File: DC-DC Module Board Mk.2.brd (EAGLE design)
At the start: 177.9 x 101.7 mm, 151 parts, among them T1 FDN340P, T2 AP1117_LIN_REG, U3 LM1085IS-5.0

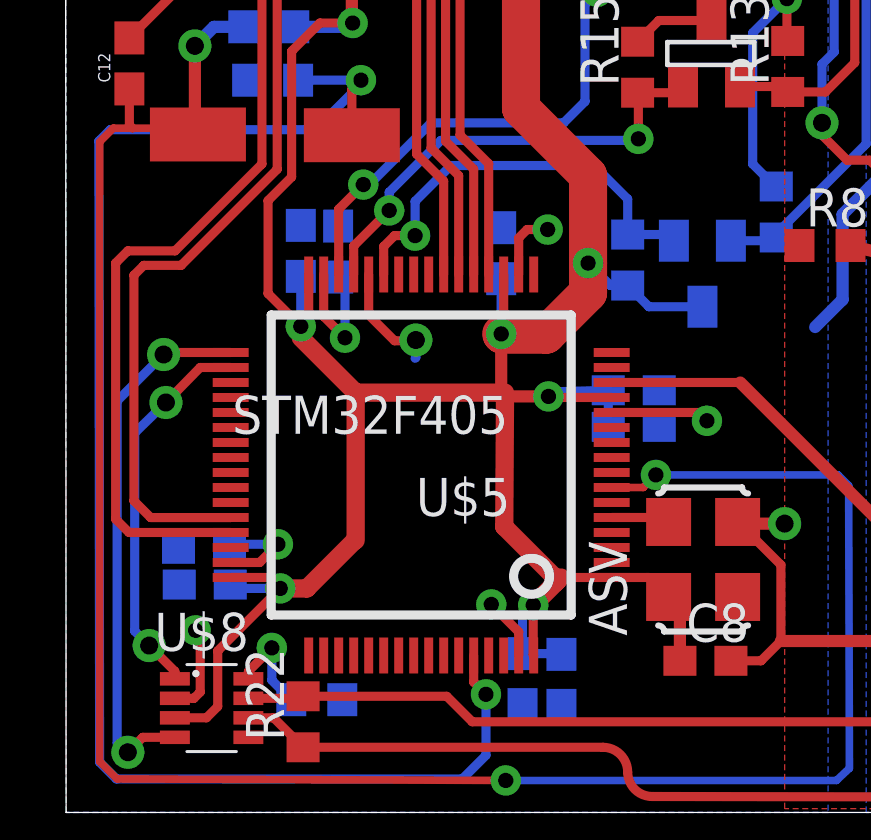
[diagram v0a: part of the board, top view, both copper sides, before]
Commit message: Changed pins for i2c
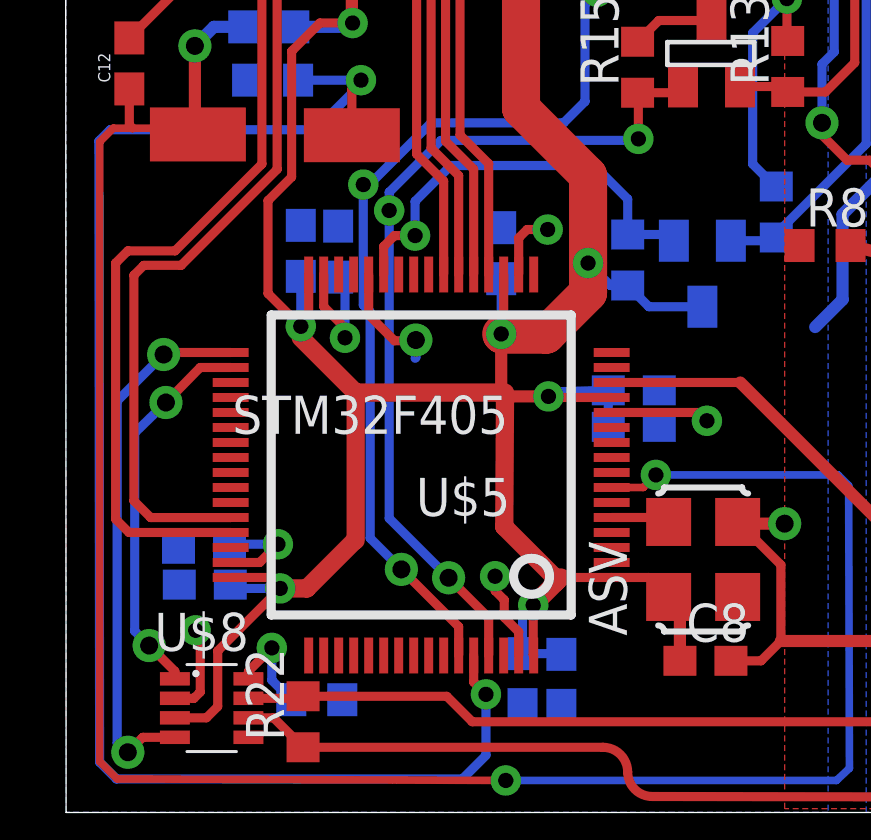
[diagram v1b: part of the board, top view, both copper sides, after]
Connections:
- removed net PB7: U$5.59
- removed net PIN61: U$5.61
- new net PB10: U$5.29
- new net PB11: U$5.30
- net SCL1: now also U$5.61; no longer U$5.29
- net SDA1: now also U$5.59; no longer U$5.30
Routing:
- net SCL1: track 15.6 -> 29.2 mm, vias 2 -> 3
- net SDA1: track 19.5 -> 33.0 mm, vias 2 -> 3
- net DGND: track 462.5 -> 463.4 mm
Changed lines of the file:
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@@
 <?xml version="1.0" encoding="utf-8"?>
 <!DOCTYPE eagle SYSTEM "eagle.dtd">
-<eagle version="7.4.0">
+<eagle version="7.5.0">
 <drawing>
 <settings>
@@
 <wire x1="4.15" y1="31.72" x2="4.15" y2="30.52" width="0.4064" layer="1"/>
 <wire x1="1.45" y1="32.02" x2="1.45" y2="34.02" width="0.4064" layer="1"/>
-<via x="14.1732" y="5.6642" extent="1-16" drill="0.508"/>
+<via x="14.3002" y="6.604" extent="1-16" drill="0.508"/>
 <wire x1="15.0864" y1="3.9624" x2="15.0864" y2="4.751" width="0.3048" layer="1"/>
-<wire x1="15.0864" y1="4.751" x2="14.1732" y2="5.6642" width="0.3048" layer="1"/>
 <wire x1="1.79" y1="39.2938" x2="1.79" y2="41.0718" width="0.3048" layer="1"/>
 <wire x1="1.79" y1="41.0718" x2="1.79" y2="42.8498" width="0.3048" layer="1"/>
@@
 <wire x1="109.9566" y1="6.1722" x2="109.982" y2="6.1976" width="0.4064" layer="1"/>
 <wire x1="109.982" y1="6.1976" x2="114.9096" y2="6.1976" width="0.4064" layer="1"/>
+<wire x1="15.0864" y1="4.751" x2="14.605" y2="5.2324" width="0.3048" layer="1"/>
+<wire x1="14.605" y1="5.2324" x2="14.605" y2="5.8166" width="0.3048" layer="1"/>
+<wire x1="14.605" y1="5.8166" x2="14.3002" y2="6.1214" width="0.3048" layer="1"/>
+<wire x1="14.3002" y1="6.1214" x2="14.3002" y2="6.604" width="0.3048" layer="1"/>
 </signal>
 <signal name="VCAP_1">
@@
 <wire x1="9.2964" y1="16.3458" x2="9.2964" y2="14.5542" width="0.3048" layer="16"/>
 <via x="9.2964" y="14.5542" extent="1-16" drill="0.508"/>
-<wire x1="9.2964" y1="14.5542" x2="8.5864" y2="15.2642" width="0.3048" layer="1"/>
-<wire x1="8.5864" y1="15.2642" x2="8.5864" y2="16.6624" width="0.3048" layer="1"/>
+<wire x1="8.5864" y1="16.6624" x2="8.5864" y2="15.5944" width="0.3048" layer="1"/>
+<wire x1="8.5864" y1="15.5944" x2="9.2964" y2="14.8844" width="0.3048" layer="1"/>
+<wire x1="9.2964" y1="14.8844" x2="9.2964" y2="14.5542" width="0.3048" layer="1"/>
 </signal>
 <signal name="VCAP_2">
@@
 <contactref element="U$5" pad="57"/>
 </signal>
-<signal name="PIN61">
-<contactref element="U$5" pad="61"/>
-</signal>
 <signal name="PIN62">
 <contactref element="U$5" pad="62"/>
@@
 <contactref element="U$9" pad="3"/>
 <contactref element="R16" pad="1"/>
-<contactref element="U$5" pad="30"/>
-<wire x1="9.0864" y1="16.6624" x2="9.0864" y2="18.84" width="0.3048" layer="1"/>
-<wire x1="9.0864" y1="18.84" x2="9.906" y2="19.6596" width="0.3048" layer="1"/>
 <via x="9.906" y="19.6596" extent="1-16" drill="0.508"/>
 <wire x1="19.2532" y1="27.5472" x2="20.636" y2="27.5472" width="0.3048" layer="1"/>
@@
 <wire x1="17.7038" y1="26.0858" x2="17.7918" y2="26.0858" width="0.3048" layer="1"/>
 <wire x1="17.7918" y1="26.0858" x2="19.2532" y2="27.5472" width="0.3048" layer="1"/>
-<wire x1="9.906" y1="19.6596" x2="10.1092" y2="19.6596" width="0.3048" layer="16"/>
 <wire x1="10.1092" y1="19.6596" x2="12.1666" y2="21.717" width="0.3048" layer="16"/>
 <wire x1="12.1666" y1="21.717" x2="16.5862" y2="21.717" width="0.3048" layer="16"/>
 <wire x1="16.5862" y1="21.717" x2="17.2974" y2="22.4282" width="0.3048" layer="16"/>
+<contactref element="U$5" pad="59"/>
+<wire x1="13.0864" y1="3.9624" x2="13.0864" y2="4.9222" width="0.3048" layer="1"/>
+<wire x1="13.0864" y1="4.9222" x2="11.176" y2="6.8326" width="0.3048" layer="1"/>
+<via x="11.176" y="6.8326" extent="1-16" drill="0.6"/>
+<wire x1="11.176" y1="6.8326" x2="10.1346" y2="7.874" width="0.3048" layer="16"/>
+<wire x1="10.1346" y1="7.874" x2="10.1346" y2="15.4178" width="0.3048" layer="16"/>
+<wire x1="10.1346" y1="15.4178" x2="9.906" y2="15.6464" width="0.3048" layer="16"/>
+<wire x1="9.906" y1="15.6464" x2="9.906" y2="19.6596" width="0.3048" layer="16"/>
+<wire x1="9.906" y1="19.6596" x2="10.1092" y2="19.6596" width="0" layer="19" extent="16-16"/>
 </signal>
 <signal name="SCL1">
 <contactref element="BSS138" pad="3"/>
 <contactref element="R15" pad="1"/>
-<contactref element="U$5" pad="29"/>
-<wire x1="9.5864" y1="16.6624" x2="9.5864" y2="17.6128" width="0.3048" layer="1"/>
-<wire x1="9.5864" y1="17.6128" x2="10.7696" y2="18.796" width="0.3048" layer="1"/>
 <via x="10.7696" y="18.796" extent="1-16" drill="0.508"/>
 <wire x1="19.05" y1="22.7212" x2="19.1906" y2="22.7212" width="0.3048" layer="1"/>
@@
 <wire x1="12.4968" y1="21.1328" x2="19.0246" y2="21.1328" width="0.3048" layer="16"/>
 <wire x1="19.0246" y1="21.1328" x2="19.0754" y2="21.1836" width="0.3048" layer="16"/>
+<contactref element="U$5" pad="61"/>
+<wire x1="14.0864" y1="3.9624" x2="14.0864" y2="5.2176" width="0.3048" layer="1"/>
+<wire x1="14.0864" y1="5.2176" x2="12.7508" y2="6.5532" width="0.3048" layer="1"/>
+<via x="12.7508" y="6.5532" extent="1-16" drill="0.6"/>
+<wire x1="12.7508" y1="6.5532" x2="10.7696" y2="8.5344" width="0.3048" layer="16"/>
+<wire x1="10.7696" y1="8.5344" x2="10.7696" y2="18.796" width="0.3048" layer="16"/>
 </signal>
 <signal name="N$63">
@@
 <contactref element="U$5" pad="58"/>
 </signal>
-<signal name="PB7">
-<contactref element="U$5" pad="59"/>
+<signal name="PB10">
+<contactref element="U$5" pad="29"/>
+</signal>
+<signal name="PB11">
+<contactref element="U$5" pad="30"/>
 </signal>
 </signals>

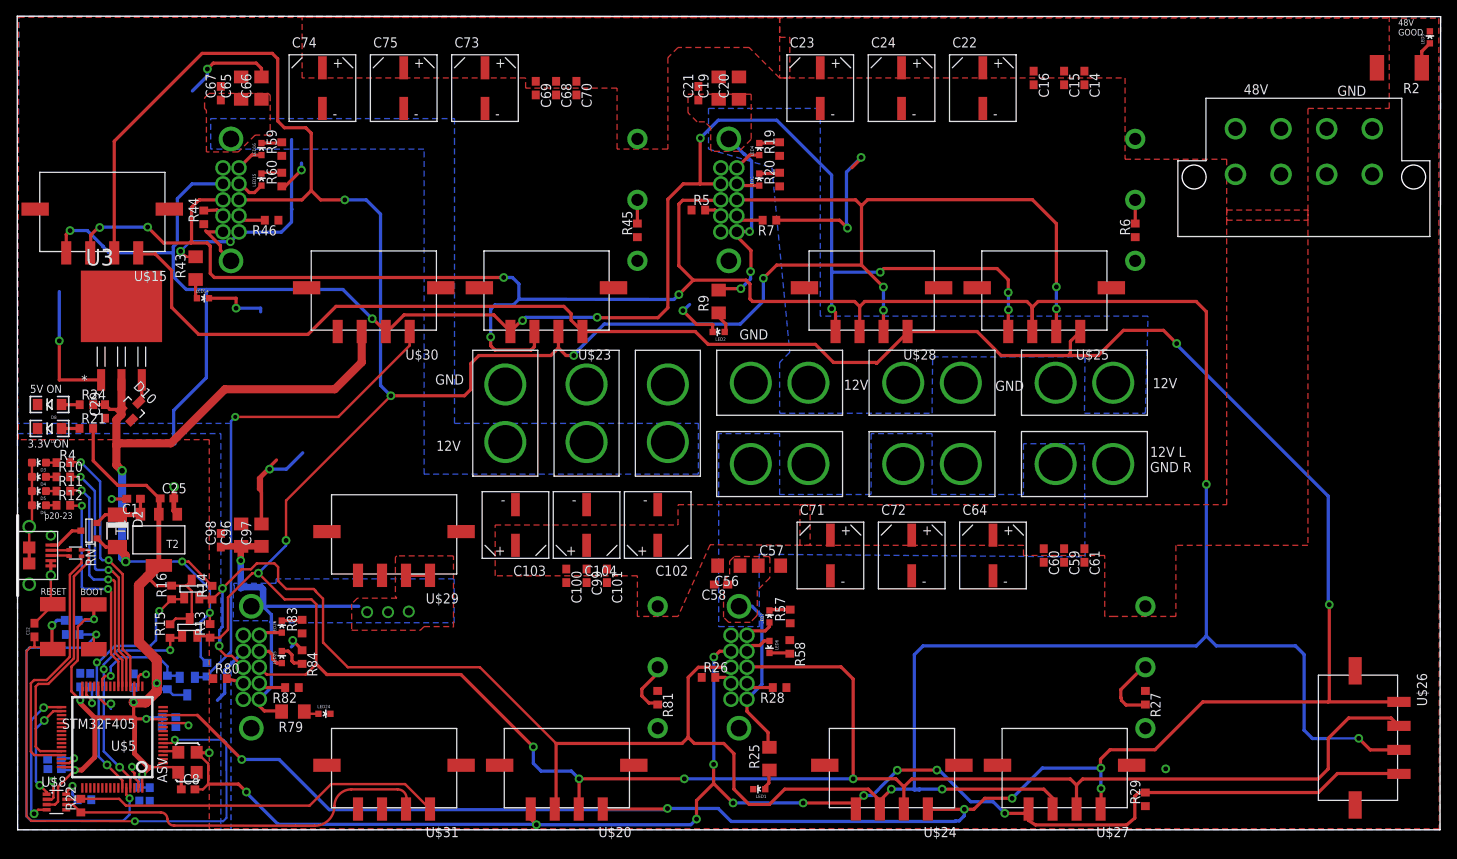
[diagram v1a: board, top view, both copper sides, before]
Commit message: Added GND vias around the board
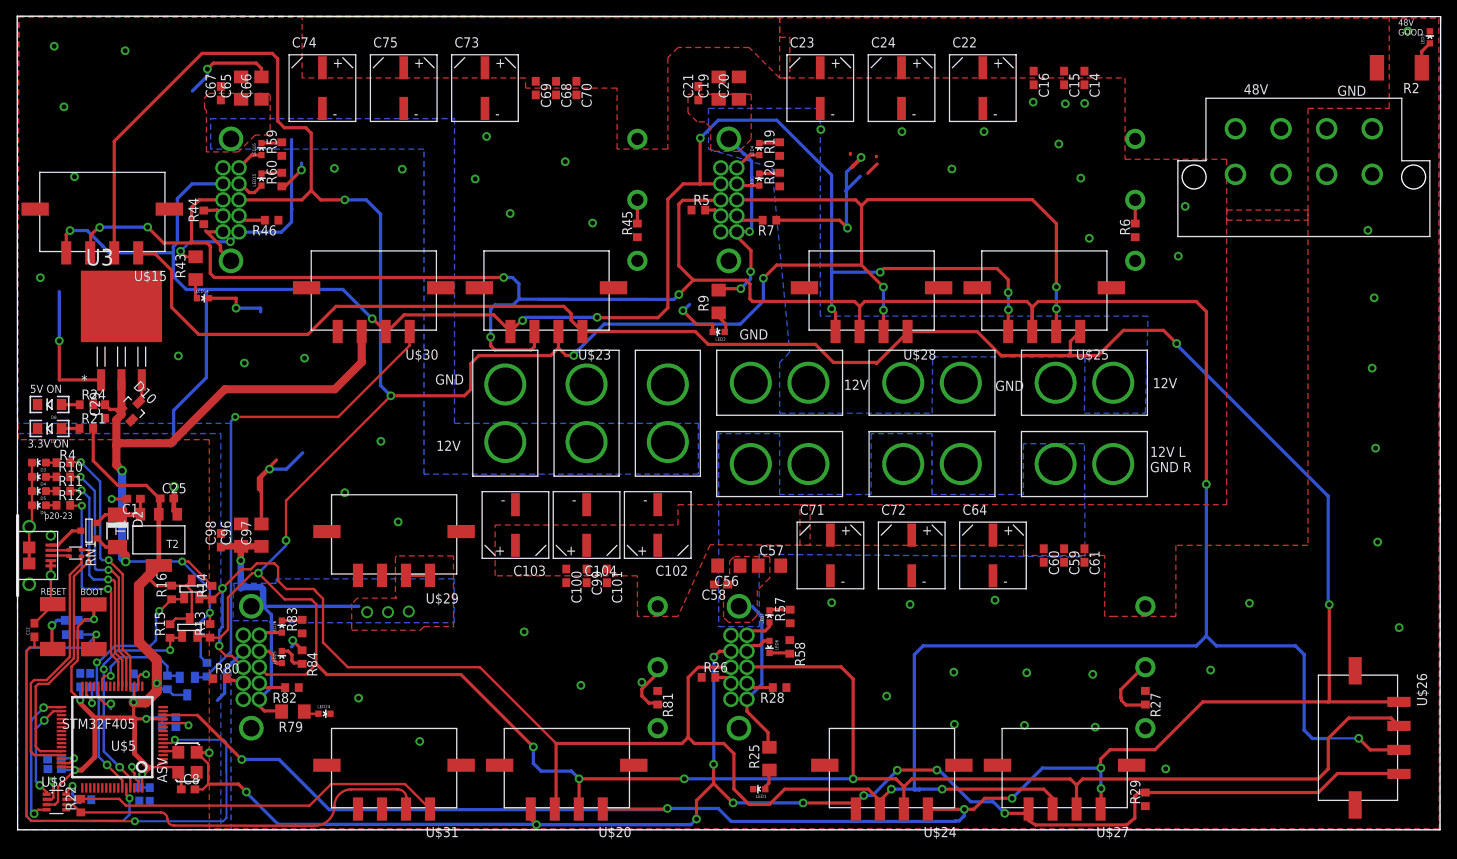
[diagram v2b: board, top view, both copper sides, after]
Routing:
- net GND: track 98.9 -> 105.1 mm, vias 9 -> 62
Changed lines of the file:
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@@
 <wire x1="103.6066" y1="80.9498" x2="105.4354" y2="82.7786" width="0.4064" layer="16"/>
 <via x="105.4354" y="82.7786" extent="1-16" drill="0.6"/>
-<wire x1="105.4354" y1="82.7786" x2="105.4354" y2="82.6516" width="0.4064" layer="1"/>
+<wire x1="105.4354" y1="82.7786" x2="105.4354" y2="82.7024" width="0.4064" layer="1"/>
+<wire x1="105.4354" y1="82.7024" x2="105.4354" y2="82.6516" width="0.4064" layer="1"/>
 <wire x1="105.4354" y1="82.6516" x2="104.267" y2="81.4832" width="0.4064" layer="1"/>
+<via x="45.4152" y="47.2948" extent="1-16" drill="0.6"/>
+<via x="40.894" y="40.8686" extent="1-16" drill="0.6"/>
+<via x="47.5742" y="37.211" extent="1-16" drill="0.6"/>
+<via x="63.3222" y="23.4696" extent="1-16" drill="0.6"/>
+<via x="70.4088" y="16.7894" extent="1-16" drill="0.6"/>
+<via x="42.6212" y="15.1892" extent="1-16" drill="0.6"/>
+<via x="50.2666" y="9.779" extent="1-16" drill="0.6"/>
+<via x="101.7524" y="27.1272" extent="1-16" drill="0.6"/>
+<via x="111.5568" y="26.8986" extent="1-16" drill="0.6"/>
+<via x="122.174" y="27.432" extent="1-16" drill="0.6"/>
+<via x="108.6358" y="15.4432" extent="1-16" drill="0.6"/>
+<via x="117.0178" y="18.4404" extent="1-16" drill="0.6"/>
+<via x="126.1364" y="18.3642" extent="1-16" drill="0.6"/>
+<via x="134.3914" y="18.161" extent="1-16" drill="0.6"/>
+<via x="117.094" y="11.9126" extent="1-16" drill="0.6"/>
+<via x="125.857" y="11.7856" extent="1-16" drill="0.6"/>
+<via x="134.6962" y="11.557" extent="1-16" drill="0.6"/>
+<via x="149.1234" y="18.6944" extent="1-16" drill="0.6"/>
+<via x="153.9748" y="27.051" extent="1-16" drill="0.6"/>
+<via x="172.6946" y="24.003" extent="1-16" drill="0.6"/>
+<via x="170.0022" y="34.6964" extent="1-16" drill="0.6"/>
+<via x="169.7482" y="46.4312" extent="1-16" drill="0.6"/>
+<via x="169.3164" y="56.4388" extent="1-16" drill="0.6"/>
+<via x="169.5704" y="65.2272" extent="1-16" drill="0.6"/>
+<via x="168.783" y="73.66" extent="1-16" drill="0.6"/>
+<via x="173.7868" y="98.5774" extent="1-16" drill="0.6"/>
+<wire x1="107.442" y1="81.9658" x2="106.2736" y2="80.7974" width="0.4064" layer="1"/>
+<wire x1="104.0892" y1="83.2866" x2="104.0892" y2="83.1596" width="0.4064" layer="1"/>
+<wire x1="104.4448" y1="81.8134" x2="104.4448" y2="81.6864" width="0.4064" layer="1"/>
+<wire x1="105.4354" y1="82.7024" x2="104.267" y2="81.534" width="0.4064" layer="1"/>
+<via x="100.4062" y="86.2584" extent="1-16" drill="0.6"/>
+<via x="110.5408" y="86.0044" extent="1-16" drill="0.6"/>
+<via x="120.8024" y="86.0044" extent="1-16" drill="0.6"/>
+<via x="126.9492" y="89.6874" extent="1-16" drill="0.6"/>
+<via x="130.9624" y="89.4842" extent="1-16" drill="0.6"/>
+<via x="133.3754" y="89.535" extent="1-16" drill="0.6"/>
+<via x="130.1496" y="84.455" extent="1-16" drill="0.6"/>
+<via x="116.7892" y="81.3308" extent="1-16" drill="0.6"/>
+<via x="132.8928" y="80.1878" extent="1-16" drill="0.6"/>
+<via x="133.9596" y="72.6694" extent="1-16" drill="0.6"/>
+<via x="145.0848" y="70.4342" extent="1-16" drill="0.6"/>
+<via x="145.9484" y="76.6572" extent="1-16" drill="0.6"/>
+<wire x1="107.3404" y1="82.931" x2="107.3404" y2="82.8548" width="0.4064" layer="1"/>
+<wire x1="103.505" y1="78.5876" x2="105.3338" y2="80.4164" width="0.4064" layer="16"/>
+<via x="58.6232" y="85.3948" extent="1-16" drill="0.6"/>
+<via x="48.0822" y="81.3054" extent="1-16" drill="0.6"/>
+<via x="39.5986" y="81.407" extent="1-16" drill="0.6"/>
+<via x="57.2008" y="80.0862" extent="1-16" drill="0.6"/>
+<via x="61.5696" y="75.7682" extent="1-16" drill="0.6"/>
+<via x="68.453" y="82.2452" extent="1-16" drill="0.6"/>
+<via x="71.882" y="74.5744" extent="1-16" drill="0.6"/>
+<via x="4.572" y="96.6724" extent="1-16" drill="0.6"/>
+<via x="13.4366" y="96.1136" extent="1-16" drill="0.6"/>
+<via x="5.7912" y="89.1032" extent="1-16" drill="0.6"/>
+<via x="7.112" y="80.3656" extent="1-16" drill="0.6"/>
+<via x="2.8448" y="67.7418" extent="1-16" drill="0.6"/>
+<via x="20.0914" y="57.9628" extent="1-16" drill="0.6"/>
+<via x="28.3464" y="57.0738" extent="1-16" drill="0.6"/>
+<via x="35.8648" y="57.6834" extent="1-16" drill="0.6"/>
 </signal>
 <signal name="N$7">
@@
 <wire x1="17.7038" y1="26.0858" x2="17.7918" y2="26.0858" width="0.3048" layer="1"/>
 <wire x1="17.7918" y1="26.0858" x2="19.2532" y2="27.5472" width="0.3048" layer="1"/>
-<wire x1="10.1092" y1="19.6596" x2="12.1666" y2="21.717" width="0.3048" layer="16"/>
+<wire x1="10.1092" y1="19.6596" x2="10.1981" y2="19.7485" width="0.3048" layer="16"/>
+<wire x1="10.1981" y1="19.7485" x2="12.1666" y2="21.717" width="0.3048" layer="16"/>
 <wire x1="12.1666" y1="21.717" x2="16.5862" y2="21.717" width="0.3048" layer="16"/>
 <wire x1="16.5862" y1="21.717" x2="17.2974" y2="22.4282" width="0.3048" layer="16"/>
@@
 <wire x1="10.1346" y1="15.4178" x2="9.906" y2="15.6464" width="0.3048" layer="16"/>
 <wire x1="9.906" y1="15.6464" x2="9.906" y2="19.6596" width="0.3048" layer="16"/>
-<wire x1="9.906" y1="19.6596" x2="10.1092" y2="19.6596" width="0" layer="19" extent="16-16"/>
+<wire x1="9.906" y1="19.6596" x2="10.1981" y2="19.6596" width="0.3048" layer="16"/>
+<wire x1="10.1981" y1="19.6596" x2="10.1981" y2="19.7485" width="0.3048" layer="16"/>
 </signal>
 <signal name="SCL1">
@@
 <contactref element="U$5" pad="30"/>
 </signal>
+<signal name="N$14">
+<via x="78.0288" y="17.1704" extent="1-16" drill="0.6"/>
+</signal>
 </signals>
